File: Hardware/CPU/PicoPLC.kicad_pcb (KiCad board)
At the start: 2 copper layers, 43 parts, among them J1 Input cluster 0, J2 Input cluster 1, J3 Common terminals, U1 LM2576T-5

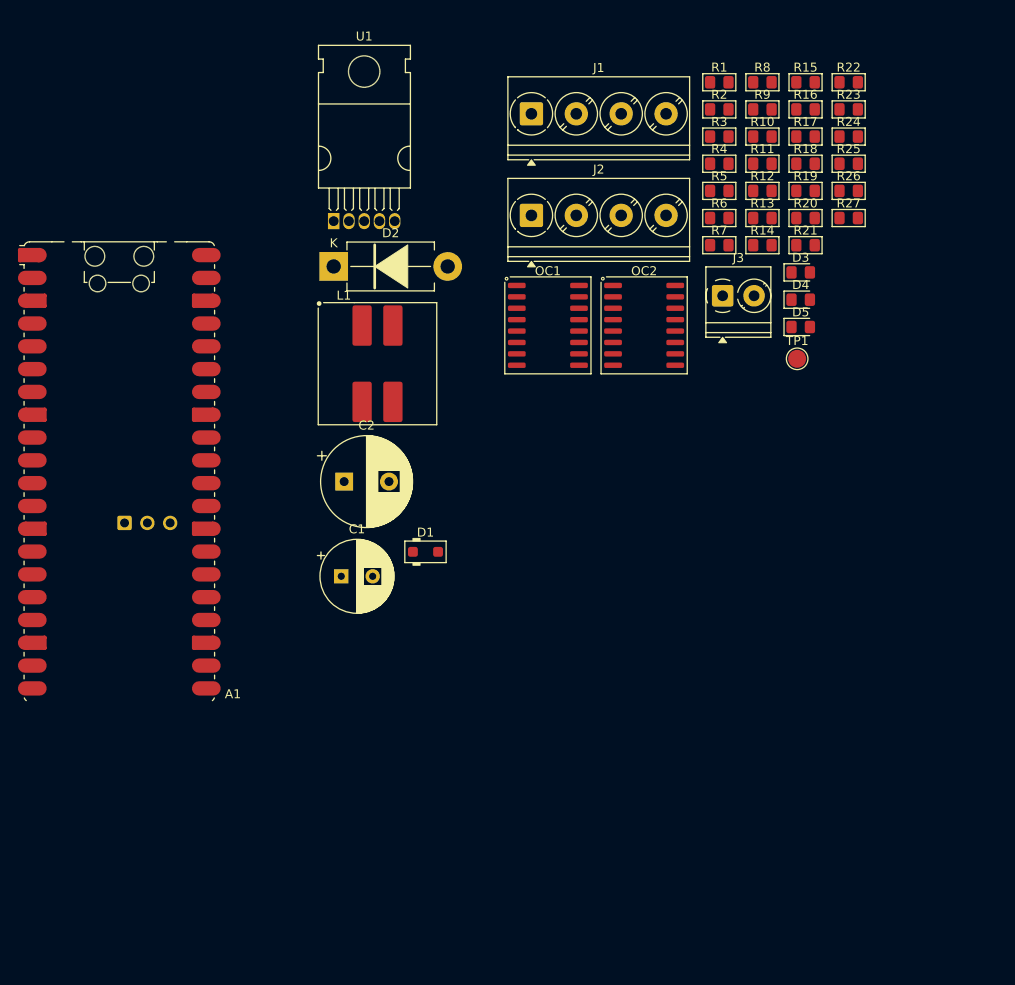
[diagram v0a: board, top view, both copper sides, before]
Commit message: finished ScreenHat Schematics
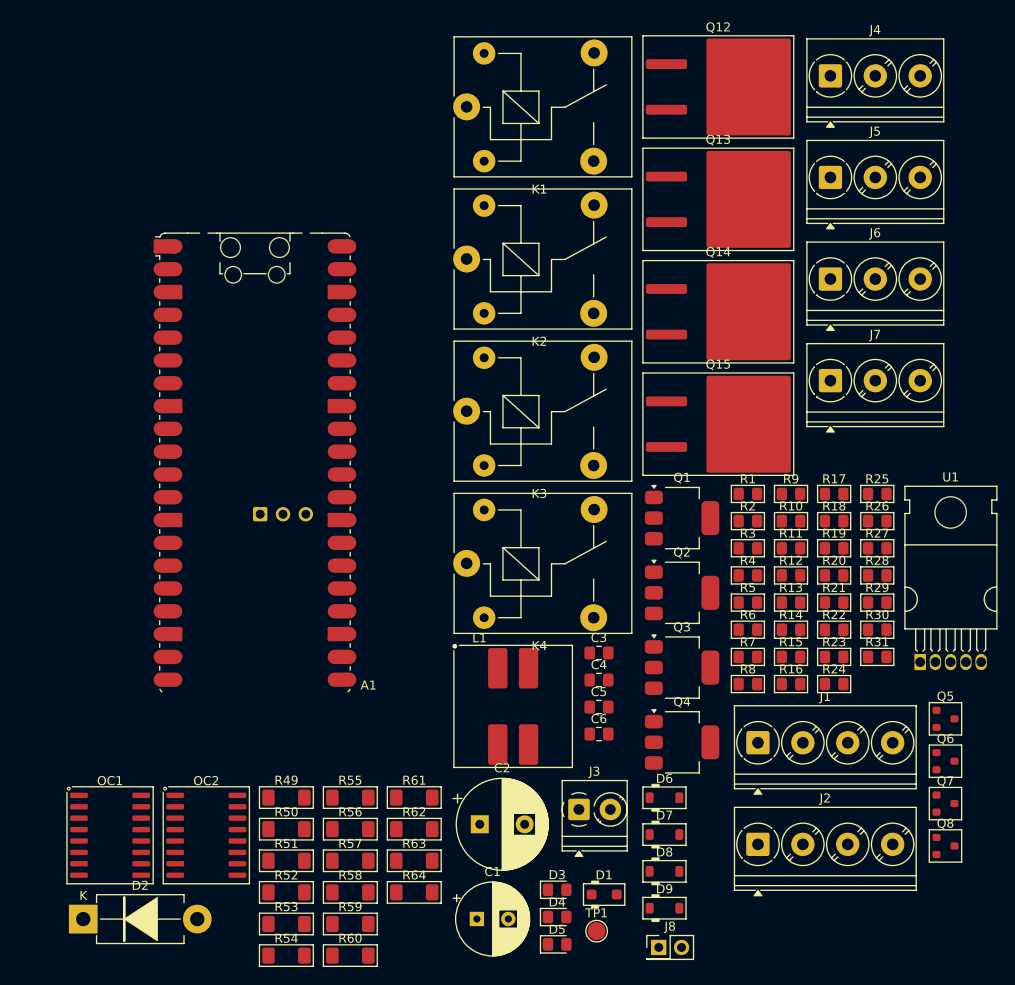
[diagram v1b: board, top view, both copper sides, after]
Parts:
- added C3: 1n, Capacitor_SMD:C_0805_2012Metric_Pad1.18x1.45mm_HandSolder, F.Cu at (106.9, 106.8)
- added C4: 1n, Capacitor_SMD:C_0805_2012Metric_Pad1.18x1.45mm_HandSolder, F.Cu at (106.9, 109.8)
- added C5: 1n, Capacitor_SMD:C_0805_2012Metric_Pad1.18x1.45mm_HandSolder, F.Cu at (106.9, 112.8)
- added C6: 1n, Capacitor_SMD:C_0805_2012Metric_Pad1.18x1.45mm_HandSolder, F.Cu at (106.9, 115.8)
- added D6: 1N4007, PCM_Diode_SMD_AKL:D_SOD-123, F.Cu at (114.2, 122.9)
- added D7: 1N4007, PCM_Diode_SMD_AKL:D_SOD-123, F.Cu at (114.2, 127.0)
- added D8: 1N4007, PCM_Diode_SMD_AKL:D_SOD-123, F.Cu at (114.2, 131.1)
- added D9: 1N4007, PCM_Diode_SMD_AKL:D_SOD-123, F.Cu at (114.2, 135.2)
- added J4: C0 terminal, TerminalBlock_Phoenix:TerminalBlock_Phoenix_PT-1,5-3-5.0-H_1x03_P5.00mm_Horizontal, F.Cu at (132.7, 42.5)
- added J5: C1 terminal, TerminalBlock_Phoenix:TerminalBlock_Phoenix_PT-1,5-3-5.0-H_1x03_P5.00mm_Horizontal, F.Cu at (132.7, 53.8)
- added J6: C2 terminal, TerminalBlock_Phoenix:TerminalBlock_Phoenix_PT-1,5-3-5.0-H_1x03_P5.00mm_Horizontal, F.Cu at (132.7, 65.1)
- added J7: C3 terminal, TerminalBlock_Phoenix:TerminalBlock_Phoenix_PT-1,5-3-5.0-H_1x03_P5.00mm_Horizontal, F.Cu at (132.7, 76.4)
- added J8: Conn_02x01, Connector_PinHeader_2.54mm:PinHeader_2x01_P2.54mm_Vertical, F.Cu at (113.6, 139.6)
- added K1: SANYOU_SRD_Form_C, Relay_THT:Relay_SPDT_SANYOU_SRD_Series_Form_C, F.Cu at (92.2, 45.9)
- added K2: SANYOU_SRD_Form_C, Relay_THT:Relay_SPDT_SANYOU_SRD_Series_Form_C, F.Cu at (92.2, 62.9)
- added K3: SANYOU_SRD_Form_C, Relay_THT:Relay_SPDT_SANYOU_SRD_Series_Form_C, F.Cu at (92.2, 79.8)
- added K4: SANYOU_SRD_Form_C, Relay_THT:Relay_SPDT_SANYOU_SRD_Series_Form_C, F.Cu at (92.2, 96.8)
- added Q1: PZT2222A, Package_TO_SOT_SMD:SOT-223-3_TabPin2, F.Cu at (116.2, 91.7)
- added Q12: IRFZ44NS, PCM_Package_TO_SOT_SMD_AKL:TO-263-2, F.Cu at (120.2, 43.7)
- added Q13: IRFZ44NS, PCM_Package_TO_SOT_SMD_AKL:TO-263-2, F.Cu at (120.2, 56.2)
- added Q14: IRFZ44NS, PCM_Package_TO_SOT_SMD_AKL:TO-263-2, F.Cu at (120.2, 68.8)
- added Q15: IRFZ44NS, PCM_Package_TO_SOT_SMD_AKL:TO-263-2, F.Cu at (120.2, 81.3)
- added Q2: PZT2222A, Package_TO_SOT_SMD:SOT-223-3_TabPin2, F.Cu at (116.2, 100.1)
- added Q3: PZT2222A, Package_TO_SOT_SMD:SOT-223-3_TabPin2, F.Cu at (116.2, 108.4)
- added Q4: PZT2222A, Package_TO_SOT_SMD:SOT-223-3_TabPin2, F.Cu at (116.2, 116.7)
- added Q5: BC847C, PCM_Package_TO_SOT_SMD_AKL:SOT-23, F.Cu at (145.5, 114.1)
- added Q6: BC847C, PCM_Package_TO_SOT_SMD_AKL:SOT-23, F.Cu at (145.5, 118.8)
- added Q7: BC847C, PCM_Package_TO_SOT_SMD_AKL:SOT-23, F.Cu at (145.5, 123.5)
- added Q8: BC847C, PCM_Package_TO_SOT_SMD_AKL:SOT-23, F.Cu at (145.5, 128.3)
- added R28: 5k, PCM_Resistor_SMD_AKL:R_0805_2012Metric_Pad1.15x1.40mm_HandSolder, F.Cu at (137.9, 98.1)
- added R29: 5k, PCM_Resistor_SMD_AKL:R_0805_2012Metric_Pad1.15x1.40mm_HandSolder, F.Cu at (137.9, 101.2)
- added R30: 5k, PCM_Resistor_SMD_AKL:R_0805_2012Metric_Pad1.15x1.40mm_HandSolder, F.Cu at (137.9, 104.2)
- added R31: 5k, PCM_Resistor_SMD_AKL:R_0805_2012Metric_Pad1.15x1.40mm_HandSolder, F.Cu at (137.9, 107.2)
- added R49: 1k, PCM_Resistor_SMD_AKL:R_1806_4516Metric, F.Cu at (72.1, 122.9)
- added R50: 10k, PCM_Resistor_SMD_AKL:R_1806_4516Metric, F.Cu at (72.1, 126.4)
- added R51: 10k, PCM_Resistor_SMD_AKL:R_1806_4516Metric, F.Cu at (72.1, 129.9)
- added R52: 10k, PCM_Resistor_SMD_AKL:R_1806_4516Metric, F.Cu at (72.1, 133.4)
- added R53: 1k, PCM_Resistor_SMD_AKL:R_1806_4516Metric, F.Cu at (72.1, 136.9)
- added R54: 10k, PCM_Resistor_SMD_AKL:R_1806_4516Metric, F.Cu at (72.1, 140.5)
- added R55: 10k, PCM_Resistor_SMD_AKL:R_1806_4516Metric, F.Cu at (79.2, 122.9)
- added R56: 10k, PCM_Resistor_SMD_AKL:R_1806_4516Metric, F.Cu at (79.2, 126.4)
- added R57: 1k, PCM_Resistor_SMD_AKL:R_1806_4516Metric, F.Cu at (79.2, 129.9)
- added R58: 10k, PCM_Resistor_SMD_AKL:R_1806_4516Metric, F.Cu at (79.2, 133.4)
- added R59: 10k, PCM_Resistor_SMD_AKL:R_1806_4516Metric, F.Cu at (79.2, 136.9)
- added R60: 10k, PCM_Resistor_SMD_AKL:R_1806_4516Metric, F.Cu at (79.2, 140.5)
- added R61: 1k, PCM_Resistor_SMD_AKL:R_1806_4516Metric, F.Cu at (86.3, 122.9)
- added R62: 10k, PCM_Resistor_SMD_AKL:R_1806_4516Metric, F.Cu at (86.3, 126.4)
- added R63: 10k, PCM_Resistor_SMD_AKL:R_1806_4516Metric, F.Cu at (86.3, 129.9)
- added R64: 10k, PCM_Resistor_SMD_AKL:R_1806_4516Metric, F.Cu at (86.3, 133.4)
- moved U1 81.7 mm to (142.7, 107.8)
- moved D2 77.9 mm to (49.5, 136.4)
- moved OC1 74.9 mm to (52.5, 127.1)
- moved OC2 74.9 mm to (63.2, 127.1)
- moved J1 74.5 mm to (124.6, 116.8)
- moved J2 74.5 mm to (124.6, 128.1)
- moved D4 73.9 mm to (102.3, 136.2)
- moved D5 73.9 mm to (102.3, 139.2)
- moved D3 73.9 mm to (102.3, 133.1)
- moved TP1 67.5 mm to (106.7, 137.7)
- moved R8 67.0 mm to (123.5, 110.2)
- moved R16 64.0 mm to (128.3, 110.2)
- moved R15 64.0 mm to (128.3, 107.2)
- moved R23 61.0 mm to (133.1, 107.2)
- moved R24 61.0 mm to (133.1, 110.2)
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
